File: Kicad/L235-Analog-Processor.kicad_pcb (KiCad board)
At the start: 2 copper layers, 110 x 110 mm, 301 parts, among them J1 Input A, J10 Half Wave A + -B, J11 Inverted Out B, J12 CV Select, J13 CV Select, J14 Conn_01x20_Pin, J15 Inverted Out A, J16 Full-Wave Rectifier A, J17 Half-Wave Rectifier A, J18 √(A²+B²), J19 Conn_01x20_Socket, J2 Input B, J3 Function IN, J4 ( 10A / |B| ) / ( A * B / 10 ), J5 Output F(x), J6 Power, J7 Full-Wave Rectifier B, J8 A - B, J9 Negative Half-Wave Rectifier B, U1 TL082, U10 TL082, U11 TL082, U12 TL082, U13 TL084, U14 RC4580, U15 TL082, U16 AD633ARZ-RL, U17 TL082, U18 LM4040DBZ-10, U19 74HC148, U2 TL082, U20 LM339, U21 LM339, U22 DG4051E, U23 DG4051E, U24 DG4051E, U25 DG4051E, U26 DG4051E, U27 74LS151, U28 DG4051E, U29 LM339, U3 TL082, U30 LM339, U31 74HC148, U32 DG4051E, U33 DG4051E, U34 DG4051E, U35 DG4051E, U36 LM78M05_TO252, U37 TL082, U4 TL082, U5 TL082, U6 TL082, U7 TL082, U8 TL082, U9 TL082

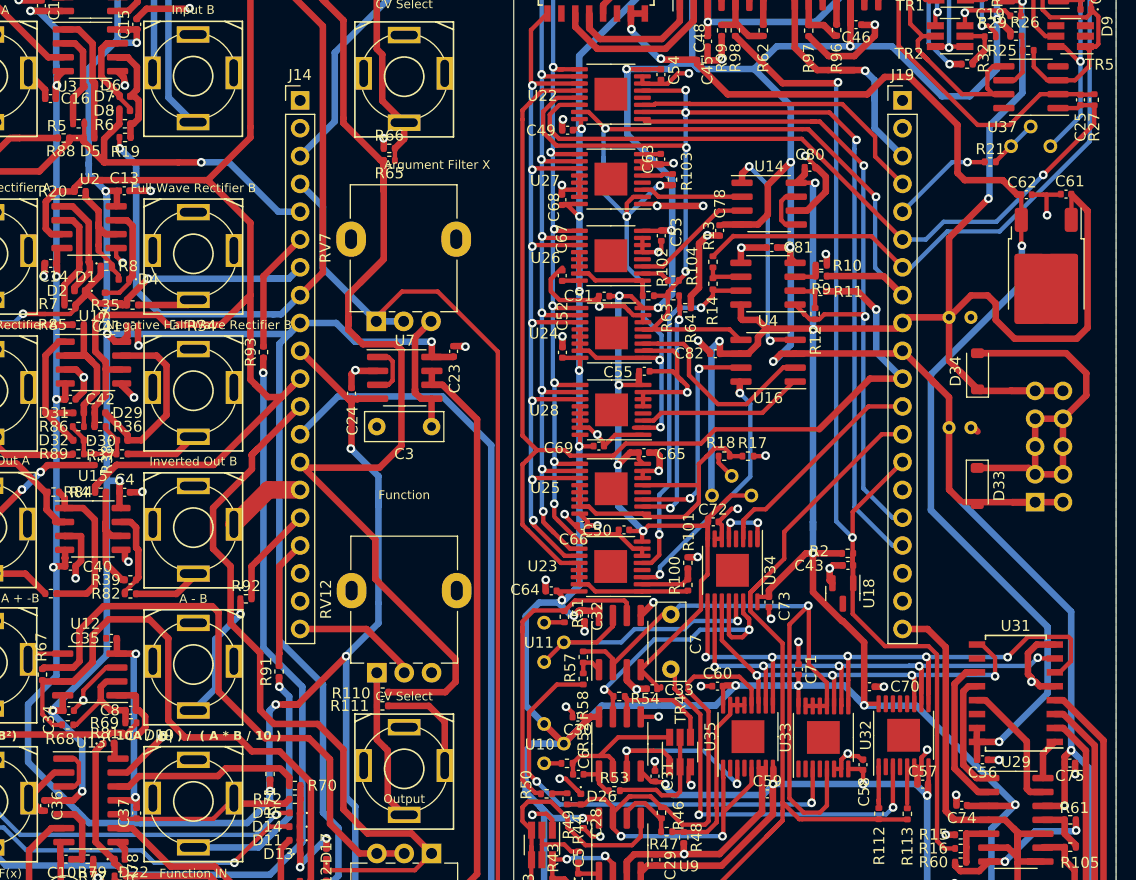
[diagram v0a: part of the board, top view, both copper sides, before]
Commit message: Fixed missing routing voltage/gnd
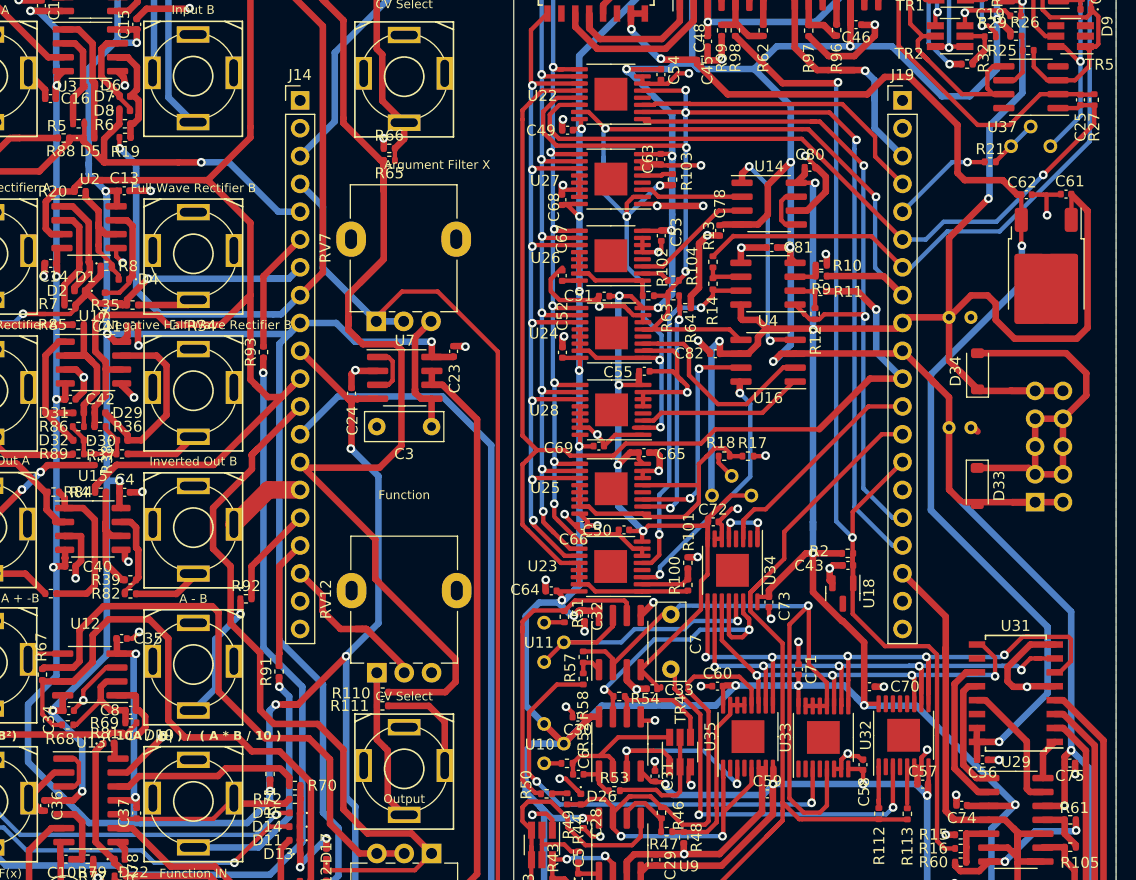
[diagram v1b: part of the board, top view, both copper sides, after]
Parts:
- moved C35 0.94 mm to (321.7, 75.6), turned to 180 degrees
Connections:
- J14 pad 18: GND -> CV_FUNCTION
- J14 pad 20: CV_FUNCTION -> unconnected-(J14-Pin_20-Pad20)
- J19 pad 18: GND -> CV_FUNCTION
- J19 pad 20: CV_FUNCTION -> unconnected-(J19-Pin_20-Pad20)
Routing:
- net CV_FUNCTION: track 65.8 -> 74.2 mm
- net GND: track 411.6 -> 418.6 mm, vias 83 -> 84
- net B1: track 51.4 -> 53.3 mm
- net -12V: track 670.4 -> 671.3 mm, vias 34 -> 35

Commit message: Added Frontpanel
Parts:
- J1: value Input A -> A INPUT
- J12: value CV Select -> CV SELECT
- J17: value Half-Wave Rectifier A -> Half-Wave Rectifier +A
- J18: value √(A²+B²) -> √A²+B²
- J2: value Input B -> B INPUT
- J4: value ( 10A / |B| ) / ( A * B / 10 ) -> A·B/10
- J5: value Output F(x) -> F(x) OUTPUT
- J9: value Negative Half-Wave Rectifier B -> Half-Wave Rectifier - B
- moved J11 182.3 mm to (148.3, 95.2)
- moved J4 182.3 mm to (148.3, 120.2)
- moved J7 182.3 mm to (148.3, 70.2)
- moved J8 182.3 mm to (148.3, 107.8)
- moved J9 182.3 mm to (148.3, 82.8)
- moved J16 182.3 mm to (129.6, 70.2)
- moved J17 182.3 mm to (129.6, 82.8)
- moved J18 182.3 mm to (129.6, 120.2)
- moved C1 182.3 mm to (229.4, 46.5)
- moved C14 182.3 mm to (135.3, 71.1)
- moved C2 182.3 mm to (231.2, 37.0)
- moved C26 182.3 mm to (184.0, 130.8)
- moved C48 182.3 mm to (194.8, 52.5)
- moved C53 182.3 mm to (191.1, 68.6)
- moved C57 182.3 mm to (214.9, 118.7)
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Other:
- board size 110 x 110 mm -> 172.9 x 128.5 mm
- board text added: "-dx/dt"
- board text added: "10"
- board text added: "100"
- board text added: "10A/|B|"
- board text added: "15"
- board text added: "20"
- board text added: "25"
- board text added: "30ms"
- board text added: "5"
- board text added: "A"
- board text added: "A - B"
- board text added: "A ATTENUATOR B"
- board text added: "ARGUMENT - X"
- board text added: "ARGUMENT FILTER"
- board text added: "A·B/10"
- board text added: "B"
- board text added: "DIRECT OUTS"
- board text added: "FUNCTION"
- board text added: "OFF"
- board text added: "OUTPUT GAIN"
- board text added: "Sine Gen."
- board text added: "X"
- board text added: "X²"
- board text added: "ln |x|"
- board text added: "√A²+B²"
- board text added: "√|x|"
- board text removed: "Argument - X"
- board text removed: "Argument Filter X"
- board text removed: "Function"
- board text removed: "Input A"
- board text removed: "Input B"
- board text removed: "Output"

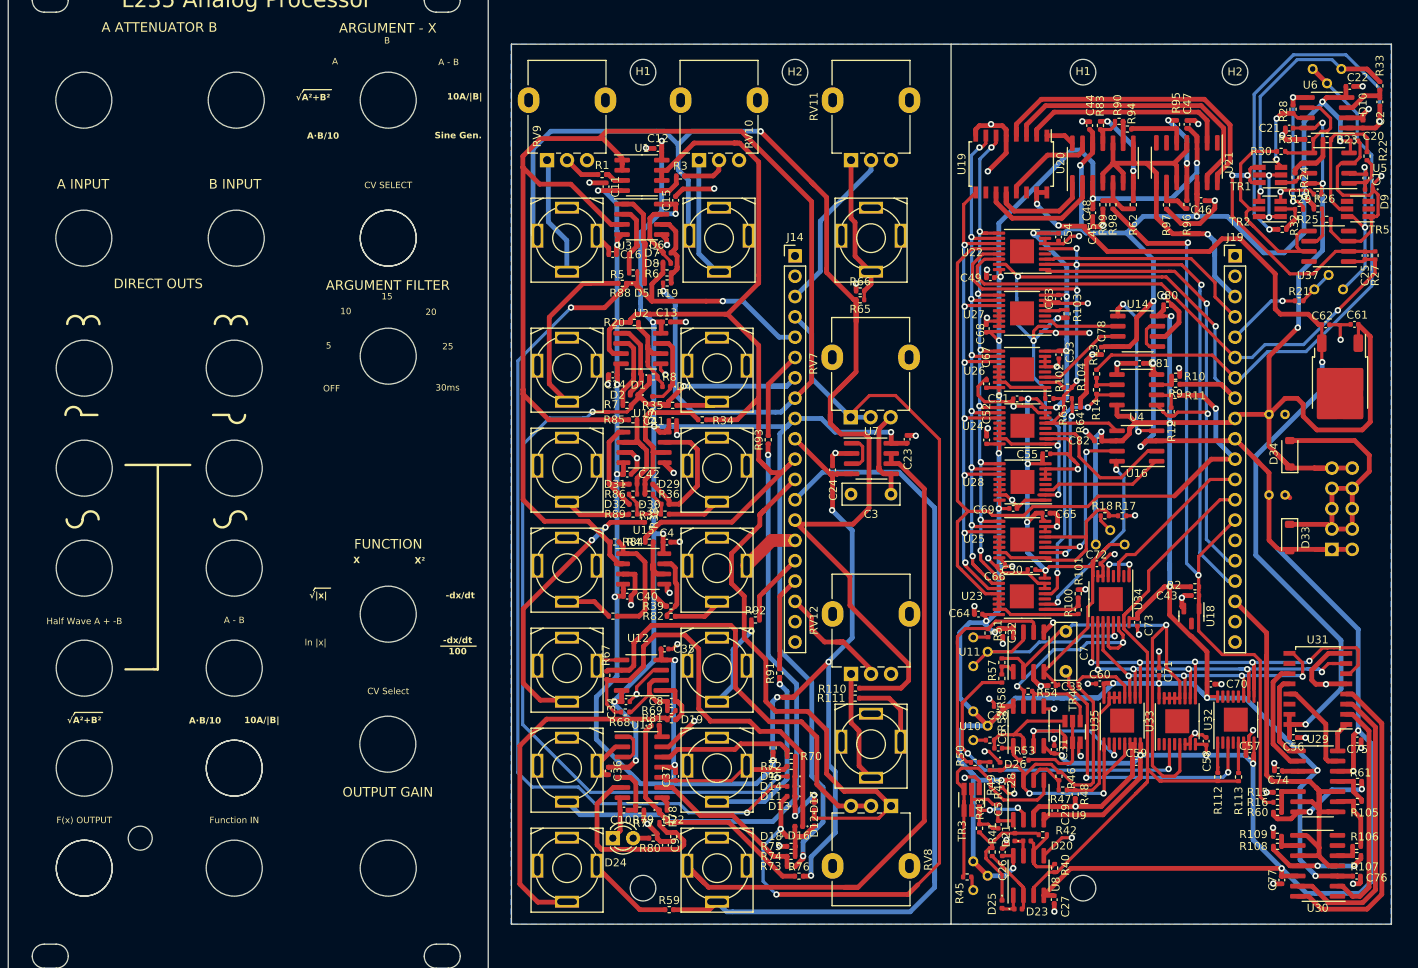
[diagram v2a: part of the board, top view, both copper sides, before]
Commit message: changed diode footprints to SOT-123
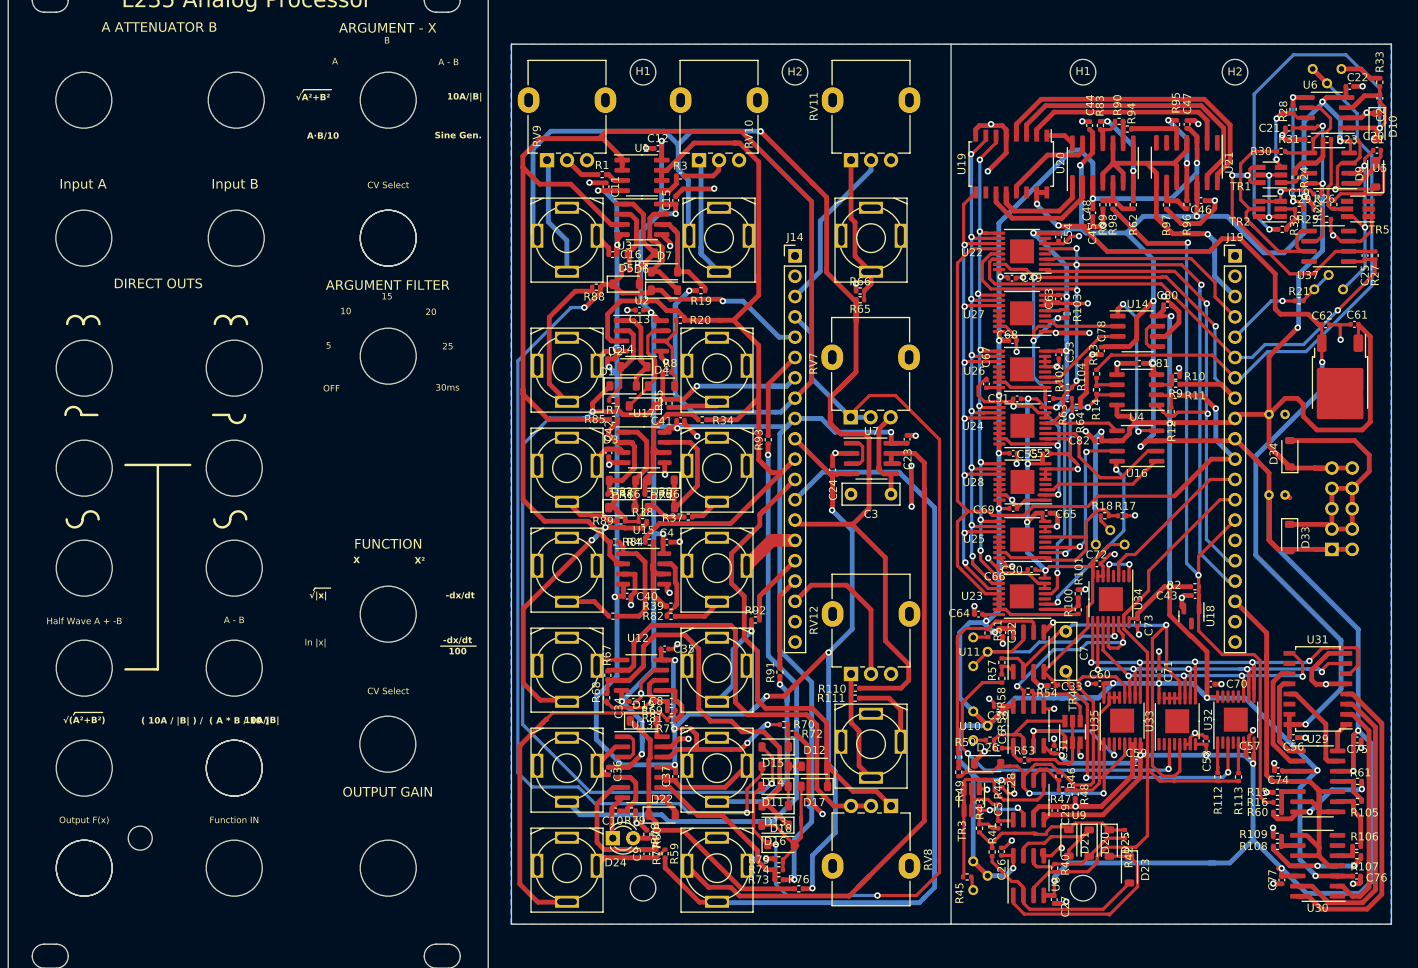
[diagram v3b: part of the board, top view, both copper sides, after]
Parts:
- removed R6: 10k, Resistor_SMD:R_0402_1005Metric
- D1, D10, D11, D12, D13, D14, D15, D16, D17, D18, D19, D2, D20, D21, D22, D23, D25, D26, D29, D3, D30, D31, D32, D4, D5, D6, D7, D8, D9: footprint Diode_SMD:D_0402_1005Metric -> Diode_SMD:D_SOD-123
- J1: value A INPUT -> Input A
- J12: value CV SELECT -> CV Select
- J17: value Half-Wave Rectifier +A -> Half-Wave Rectifier A
- J18: value √A²+B² -> √(A²+B²)
- J2: value B INPUT -> Input B
- J4: value A·B/10 -> ( 10A / |B| ) / ( A * B / 10 )
- J5: value F(x) OUTPUT -> Output F(x)
- J9: value Half-Wave Rectifier - B -> Negative Half-Wave Rectifier B
- R35, R37, R38, R82, R87, R88, R89, R91, R92, R93: value 180 -> 1k
- U22, U23, U24, U25, U26, U28: value DG4051E -> CD4051
- moved D25 15.4 mm to (197.4, 129.6)
- moved D23 14.7 mm to (199.9, 132.9), turned to -90 degrees
- moved R71 11.1 mm to (144.5, 115.3), turned to 180 degrees
- moved R42 10.2 mm to (199.3, 128.5), turned to 90 degrees
- moved D20 7.78 mm to (194.9, 129.6), turned to -90 degrees
- moved R22 7.34 mm to (225.4, 49.8), turned to -90 degrees
- moved R59 7.02 mm to (141.9, 130.9), turned to -90 degrees
- moved D21 6.79 mm to (192.3, 129.6)
- moved R20 5.76 mm to (143.8, 64.3), turned to 180 degrees
- moved D12 4.99 mm to (160.5, 120.0), turned to 0 degrees
- moved D17 4.45 mm to (160.5, 122.5), turned to 180 degrees
- moved R19 4.34 mm to (146.3, 60.6)
- moved D15 4.18 mm to (155.6, 117.6)
- moved R70 4.07 mm to (156.7, 114.8)
- moved R72 4.05 mm to (157.7, 116.0), turned to 180 degrees
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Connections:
- TR2 pad 4: Net-(R33-Pad2) -> GND
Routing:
- net Net-(R33-Pad2): track 31.1 -> 5.28 mm, vias 1 -> 0
- net Net-(D23-K): track 3.32 -> 25.2 mm
- net Net-(D23-A): track 10.3 -> 24.6 mm
- net Net-(D9-A): track 6.19 -> 19.0 mm
- net Net-(D20-K): track 2.87 -> 14.6 mm
- net Net-(D16-A): track 6.74 -> 17.9 mm
- net GND: track 418.6 -> 429.2 mm, vias 84 -> 86
- net Net-(U13B--): track 26.9 -> 18.0 mm
- net Function Out: track 91.3 -> 84.0 mm
- net B|: track 8.84 -> 16.1 mm
- net +12V: track 663.8 -> 670.7 mm
- net <X>: track 184.4 -> 190.9 mm
- net |B|: track 191.7 -> 197.8 mm
- net X²: track 60.7 -> 66.6 mm
- net Net-(D7-K): track 8.49 -> 14.1 mm
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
